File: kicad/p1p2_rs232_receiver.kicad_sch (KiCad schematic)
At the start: 65 parts, among them J1 Raspberry_Pi_2_3, J2 PC MC_1,5_2-G-3.81, Q1 BSS123, SW1 SW_Push, U1 LM4040DBZ-3, U103 LM4861, U3 Pico

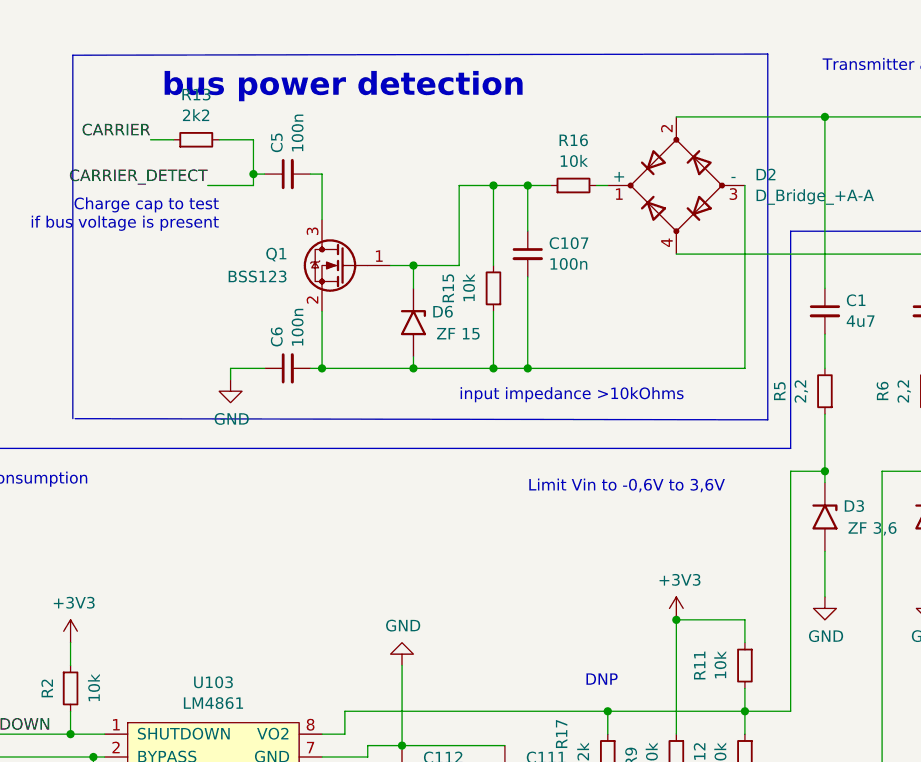
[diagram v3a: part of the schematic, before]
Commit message: kicad: Add warning texts to design
Signed-off-by: Patrick Rudolph <rudolphpatrick05@gmail.com>
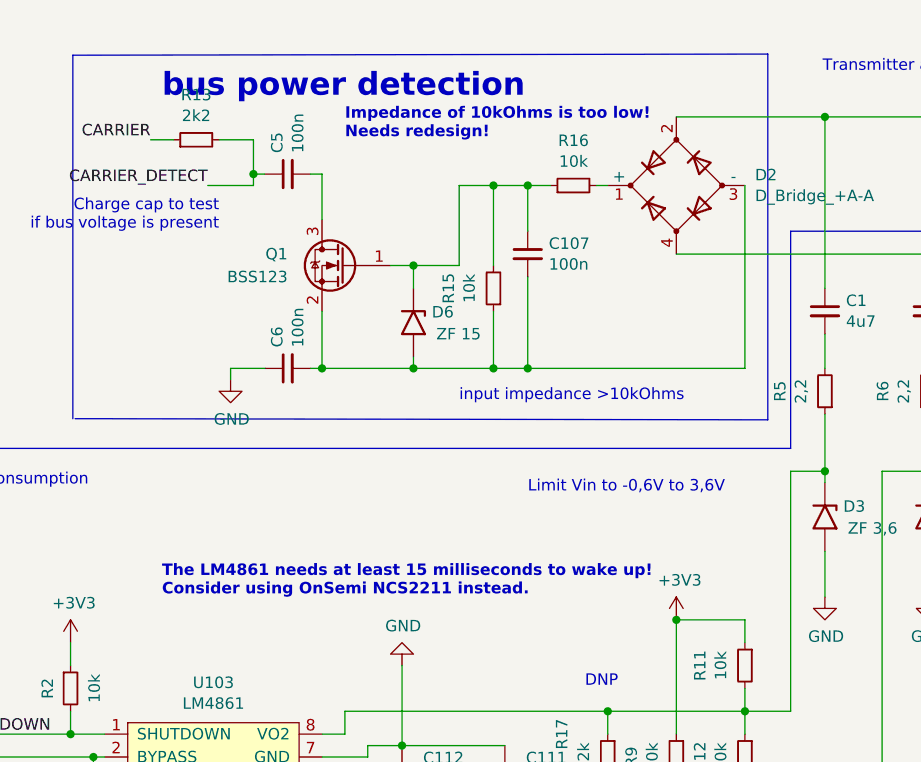
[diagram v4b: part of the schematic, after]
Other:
- note added: "Impedance of 10kOhms is too low! Needs redesign!"
- note added: "The LM4861 needs at least 15 milliseconds to wake up! Consider using OnSemi NCS2211 instead."
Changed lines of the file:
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@@
     (effects (font (size 2.54 2.54) (thickness 0.508) bold) (justify left bottom))
+  )
+  (text "The LM4861 needs at least 15 milliseconds to wake up!\nConsider using OnSemi NCS2211 instead."
+    (at 92.71 77.47 0)
+    (effects (font (size 1.27 1.27) (thickness 0.254) bold) (justify left bottom))
   )
   (text "LM4861 drives 0.5W @3.3V.\nYou can use LM4871 and drive with 0.75W @3.3V"
@@
     (effects (font (size 1.27 1.27)) (justify left bottom))
   )
+  (text "Impedance of 10kOhms is too low!\nNeeds redesign!" (at 113.03 26.67 0)
+    (effects (font (size 1.27 1.27) (thickness 0.254) bold) (justify left bottom))
+  )
   (text "Receiver" (at 190.246 111.76 0)

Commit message: kicad: Update schematics
Signed-off-by: Patrick Rudolph <rudolphpatrick05@gmail.com>
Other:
- note added: "The LM4861 needs at least 15 milliseconds to wake up! Consider using OnSemi NCS2211 instead. THe LM4861 shutdown function causes huge distortions on the output!"
- note removed: "The LM4861 needs at least 15 milliseconds to wake up! Consider using OnSemi NCS2211 instead."
- moved on the sheet: R104, R108
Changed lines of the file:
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@@
   (junction (at 241.3 25.4) (diameter 0) (color 0 0 0 0)
   )
-  (junction (at 52.07 100.33) (diameter 0) (color 0 0 0 0)
+  (junction (at 45.72 100.33) (diameter 0) (color 0 0 0 0)
   )
   (junction (at 133.35 31.75) (diameter 0) (color 0 0 0 0)
@@
   (no_connect (at 62.992 154.94))
   (no_connect (at 62.992 157.48))
-  (wire (pts (xy 52.07 96.52) (xy 52.07 100.33))
+  (wire (pts (xy 45.72 96.52) (xy 45.72 100.33))
     (stroke (width 0) (type default) (color 0 0 0 0))
   )
@@
     (stroke (width 0) (type default) (color 0 0 0 0))
   )
-  (wire (pts (xy 52.07 100.33) (xy 78.74 100.33))
+  (wire (pts (xy 45.72 100.33) (xy 78.74 100.33))
     (stroke (width 0) (type default) (color 0 0 0 0))
   )
@@
     (stroke (width 0) (type default) (color 0 0 0 0))
   )
-  (wire (pts (xy 46.99 105.41) (xy 39.37 105.41))
+  (wire (pts (xy 40.64 105.41) (xy 33.02 105.41))
     (stroke (width 0) (type default) (color 0 0 0 0))
   )
@@
     (stroke (width 0) (type default) (color 0 0 0 0))
   )
-  (wire (pts (xy 52.07 100.33) (xy 52.07 105.41))
+  (wire (pts (xy 45.72 100.33) (xy 45.72 105.41))
     (stroke (width 0) (type default) (color 0 0 0 0))
   )
@@
     (stroke (width 0) (type default) (color 0 0 0 0))
   )
-  (wire (pts (xy 39.37 96.52) (xy 46.99 96.52))
+  (wire (pts (xy 33.02 96.52) (xy 40.64 96.52))
     (stroke (width 0) (type default) (color 0 0 0 0))
   )
@@
     (effects (font (size 2.54 2.54) (thickness 0.508) bold) (justify left bottom))
   )
-  (text "The LM4861 needs at least 15 milliseconds to wake up!\nConsider using OnSemi NCS2211 instead."
-    (at 92.71 77.47 0)
+  (text "The LM4861 needs at least 15 milliseconds to wake up!\nConsider using OnSemi NCS2211 instead.\nTHe LM4861 shutdown function causes huge distortions on the output!"
+    (at 81.28 73.66 0)
     (effects (font (size 1.27 1.27) (thickness 0.254) bold) (justify left bottom))
   )
@@
     (effects (font (size 1.27 1.27)) (justify right bottom))
   )
-  (label "A_L" (at 39.37 105.41 0)
-    (effects (font (size 1.27 1.27)) (justify left bottom))
-  )
-  (label "A_H" (at 39.37 96.52 0)
+  (label "A_L" (at 33.02 105.41 0)
+    (effects (font (size 1.27 1.27)) (justify left bottom))
+  )
+  (label "A_H" (at 33.02 96.52 0)
     (effects (font (size 1.27 1.27)) (justify left bottom))
   )
@@
     (pin "1")
   )
-  (symbol (lib_id "Device:R_Small") (at 49.53 96.52 90) (unit 1)
-    (in_bom yes) (on_board yes)
-    (property "Reference" "R104" (id 0) (at 49.53 91.5416 90))
-    (property "Value" "2k2" (id 1) (at 49.53 93.853 90))
-    (property "Footprint" "Resistor_SMD:R_0805_2012Metric_Pad1.20x1.40mm_HandSolder" (id 2) (at 49.53 96.52 0)
-      (effects (font (size 1.27 1.27)) hide)
-    )
-    (property "Datasheet" "~" (id 3) (at 49.53 96.52 0)
-      (effects (font (size 1.27 1.27)) hide)
-    )
-    (pin "1")
-    (pin "2")
-  )
-  (symbol (lib_id "Device:R_Small") (at 49.53 105.41 270) (unit 1)
-    (in_bom yes) (on_board yes)
-    (property "Reference" "R108" (id 0) (at 49.53 110.3884 90))
-    (property "Value" "2k2" (id 1) (at 49.53 108.077 90))
-    (property "Footprint" "Resistor_SMD:R_0805_2012Metric_Pad1.20x1.40mm_HandSolder" (id 2) (at 49.53 105.41 0)
-      (effects (font (size 1.27 1.27)) hide)
-    )
-    (property "Datasheet" "~" (id 3) (at 49.53 105.41 0)
-      (effects (font (size 1.27 1.27)) hide)
-    )
+  (symbol (lib_id "Device:R_Small") (at 43.18 96.52 90) (unit 1)
+    (in_bom yes) (on_board yes)
+    (property "Reference" "R104" (id 0) (at 43.18 91.5416 90))
+    (property "Value" "2k2" (id 1) (at 43.18 93.853 90))
+    (property "Footprint" "Resistor_SMD:R_0805_2012Metric_Pad1.20x1.40mm_HandSolder" (id 2) (at 43.18 96.52 0)
+      (effects (font (size 1.27 1.27)) hide)
+    )
+    (property "Datasheet" "~" (id 3) (at 43.18 96.52 0)
+      (effects (font (size 1.27 1.27)) hide)
+    )
+    (pin "1")
+    (pin "2")
+  )
+  (symbol (lib_id "Device:R_Small") (at 43.18 105.41 270) (unit 1)
+    (in_bom yes) (on_board yes)
+    (property "Reference" "R108" (id 0) (at 43.18 110.3884 90))
+    (property "Value" "2k2" (id 1) (at 43.18 108.077 90))
+    (property "Footprint" "Resistor_SMD:R_0805_2012Metric_Pad1.20x1.40mm_HandSolder" (id 2) (at 43.18 105.41 0)
+      (effects (font (size 1.27 1.27)) hide)
+    )
+    (property "Datasheet" "~" (id 3) (at 43.18 105.41 0)
+      (effects (font (size 1.27 1.27)) hide)
+    )

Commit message: kicad: Redesign to TX with more power
- Use 5V as LM4871 power supply
- Decrease output impedance to 4.5 Ohms
- Decrease input impedance to 1k Ohm
- AC couple input signal

Signed-off-by: Patrick Rudolph <rudolphpatrick05@gmail.com>
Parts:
- removed C107: 100n, Capacitor_SMD:C_0805_2012Metric_Pad1.18x1.45mm_HandSolder, symbol Device:C_Small
- added C8: 100n, Capacitor_SMD:C_0805_2012Metric_Pad1.18x1.45mm_HandSolder, symbol Device:C_Small
- C1, C2: value 4u7 -> 6u8
- C4: value 4p7 -> 220p
- D3, D5: value ZF 3,6 -> ZF 5,6
- R104, R108: value 2k2 -> 1k
- R14: value 47k -> 16k
- R15: value 10k -> 100k
- R16: value 10k -> 220k
- R5, R6: value 2,2 -> 1
- U103: value LM4861 -> LM4871
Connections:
- net +3V3: no longer C111.2, C112.2, R11.1, R9.1, U103.6 (VDD)
- net +VDC: now also C111.2, C112.2, R11.1, R9.1, U103.6 (VDD)
- net at R104.2, R108.1: now also C8.1; no longer R3.1
- new net: C8.2, R3.1
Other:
- note added: "C4: Low pass filter for less overshoot/undershoot"
- note added: "LM4871 drives 3W@5.0V"
- note added: "Reset button"
- note added: "THe LM4871 shutdown function causes huge distortions on the output!"
- note added: "Vout 0,3 - 4,7V Differential amplitude: +-4,4V Pout: 3W max 4.5 Ohms output impedance"
- note removed: "Add 4p7 to prevent oscillation"
- note removed: "Impedance of 10kOhms is too low! Needs redesign!"
- note removed: "LM4861 drives 0.5W @3.3V. You can use LM4871 and drive with 0.75W @3.3V"
- note removed: "Limit Vin to -0,6V to 3,6V"
- note removed: "The LM4861 needs at least 15 milliseconds to wake up! Consider using OnSemi NCS2211 instead. THe LM4861 shutdown function causes huge distortions on the output!"
- note removed: "Vout 0,3 - 3.0V Differential amplitude: 5,2V Pout: 0.5W max 10 Ohms output impedance"
- moved on the sheet: D4, D6, R15

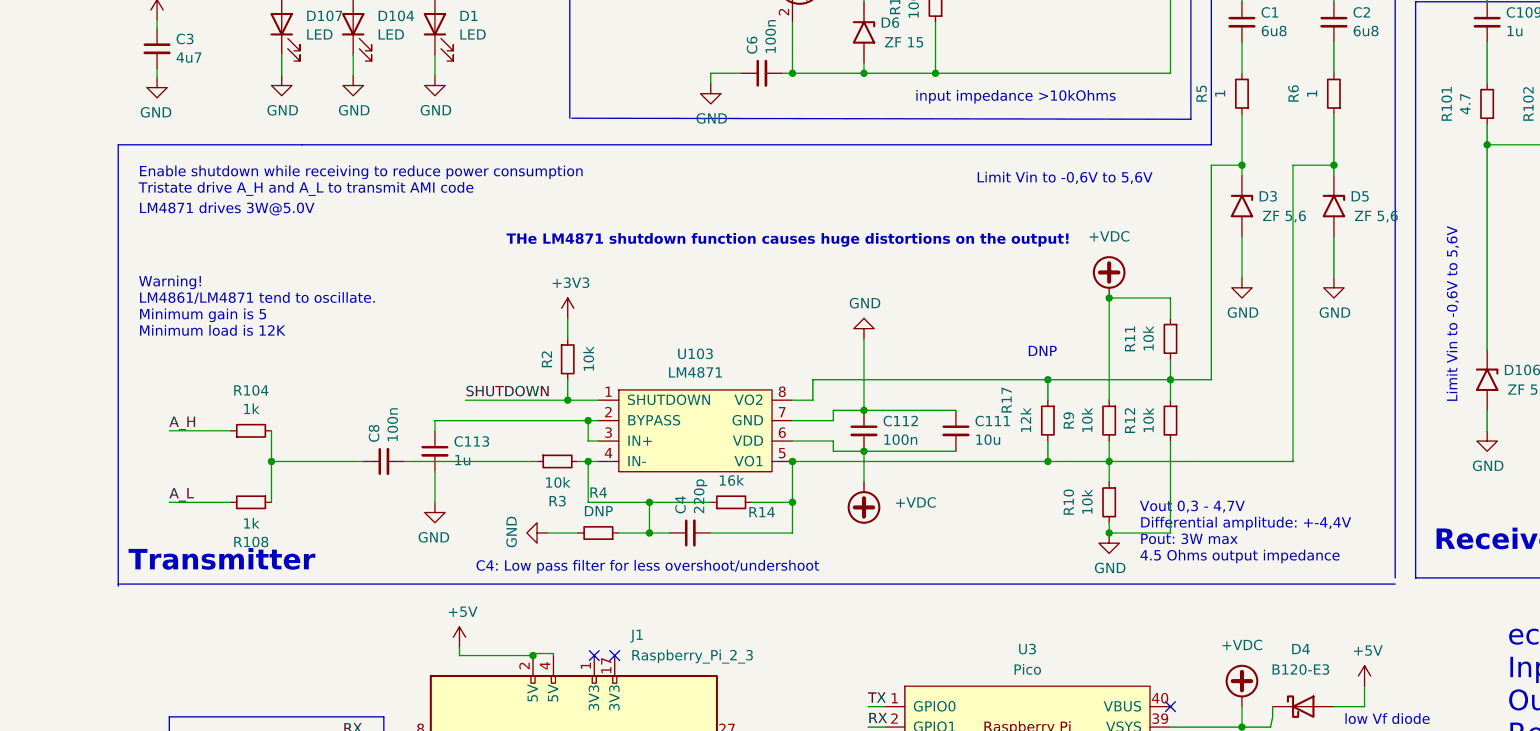
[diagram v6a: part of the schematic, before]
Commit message: kicad: Fixes for version v0.3
- Replace Ti LM4871 with STM TS4990
- Power SHUTDOWN from +5V rail
- Use double ground plane

Signed-off-by: Patrick Rudolph <rudolphpatrick05@gmail.com>
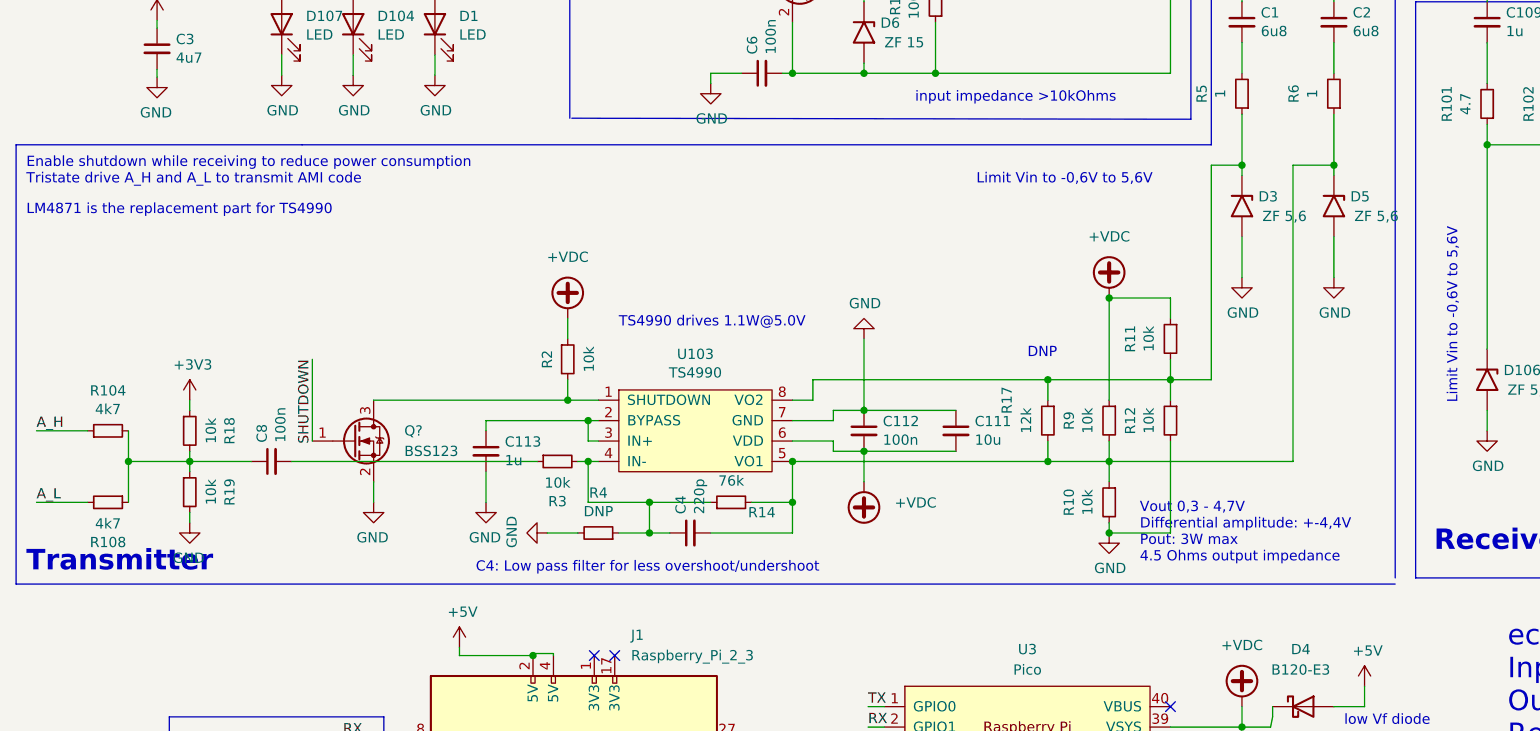
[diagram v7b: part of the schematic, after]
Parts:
- added Q?: BSS123, Package_TO_SOT_SMD:SOT-23, symbol Transistor_FET:BSS123
- added R18, R19: 10k, Resistor_SMD:R_0805_2012Metric_Pad1.20x1.40mm_HandSolder, symbol Device:R_Small
- R104, R108: value 1k -> 4k7
- R14: value 16k -> 76k
- U103: value LM4871 -> TS4990
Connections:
- net +3V3: now also R18.1; no longer R2.1
- net +VDC: now also R2.1
- net GND: now also Q?.2 (S), R19.2
- net SHUTDOWN: now also Q?.1 (G); no longer R2.2, U103.1 (SHUTDOWN)
- net at C8.1, R104.2, R108.1: now also R18.2, R19.1
- new net: Q?.3 (D), R2.2, U103.1 (SHUTDOWN)
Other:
- note added: "LM4871 is the replacement part for TS4990"
- note added: "TS4990 drives 1.1W@5.0V"
- note removed: "LM4871 drives 3W@5.0V"
- note removed: "THe LM4871 shutdown function causes huge distortions on the output!"
- note removed: "Warning! LM4861/LM4871 tend to oscillate. Minimum gain is 5 Minimum load is 12K"
- moved on the sheet: C113, C8, R104, R108
